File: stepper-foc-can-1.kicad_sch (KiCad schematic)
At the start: 33 parts, among them J1 TC2030, J2 Conn_01x02, J4 Conn_01x04_Pin, U1 STM32G474RBTx, U2 MX25947, Y1 Crystal_GND24

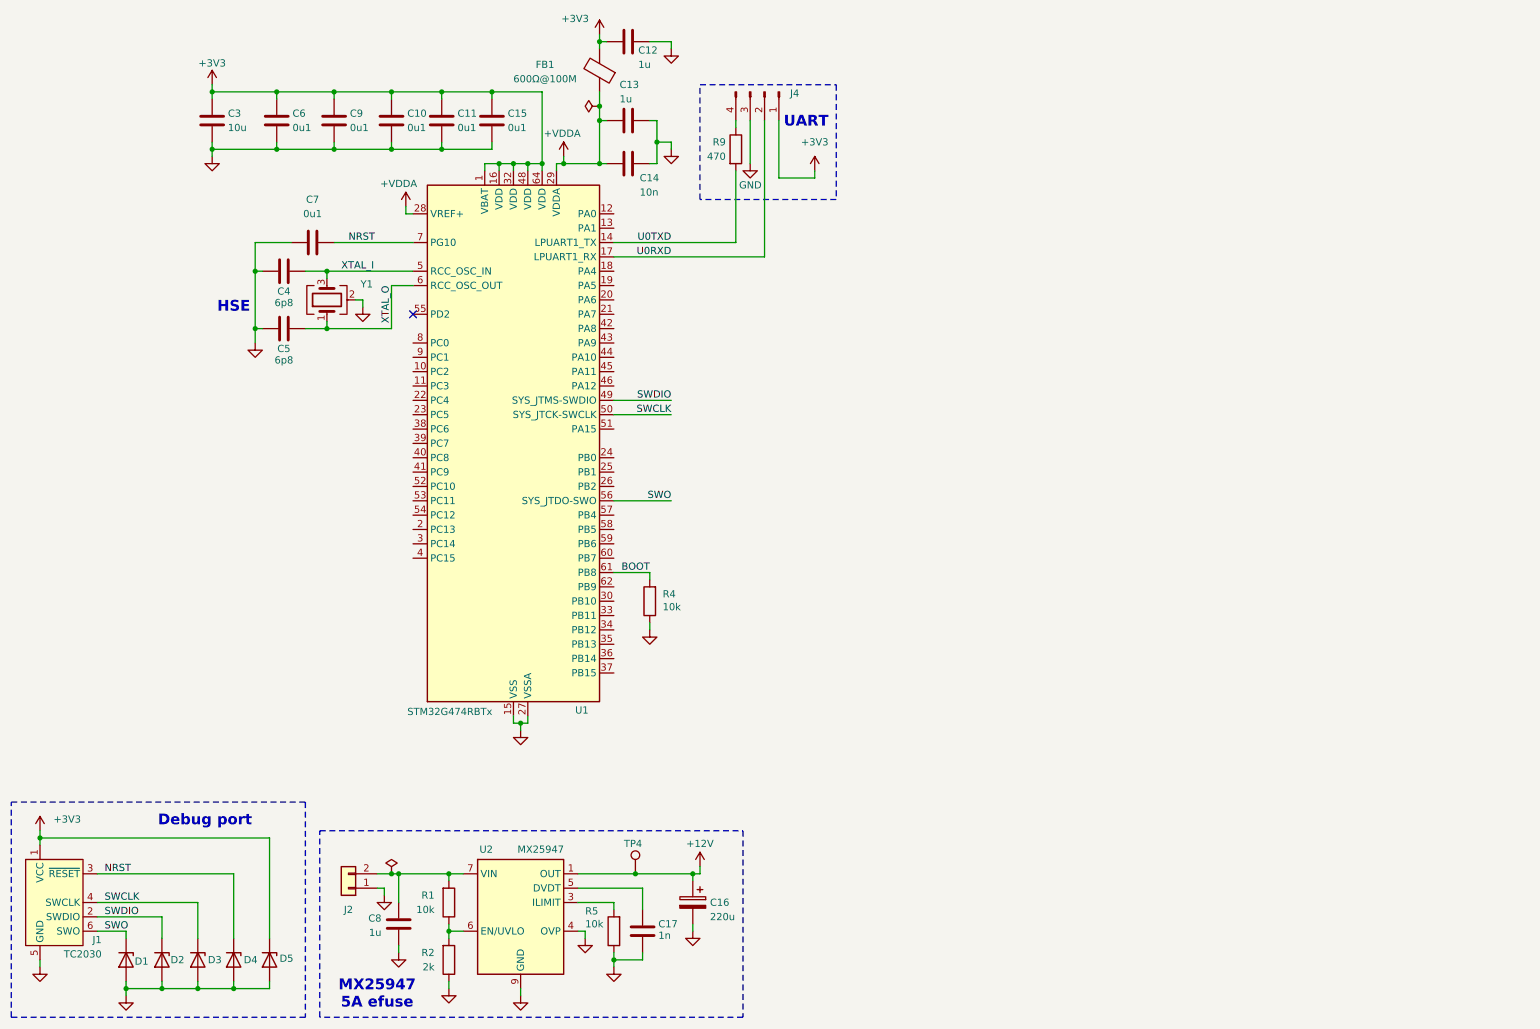
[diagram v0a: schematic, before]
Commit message: schem: import TCAN3413 CAN Transceiver
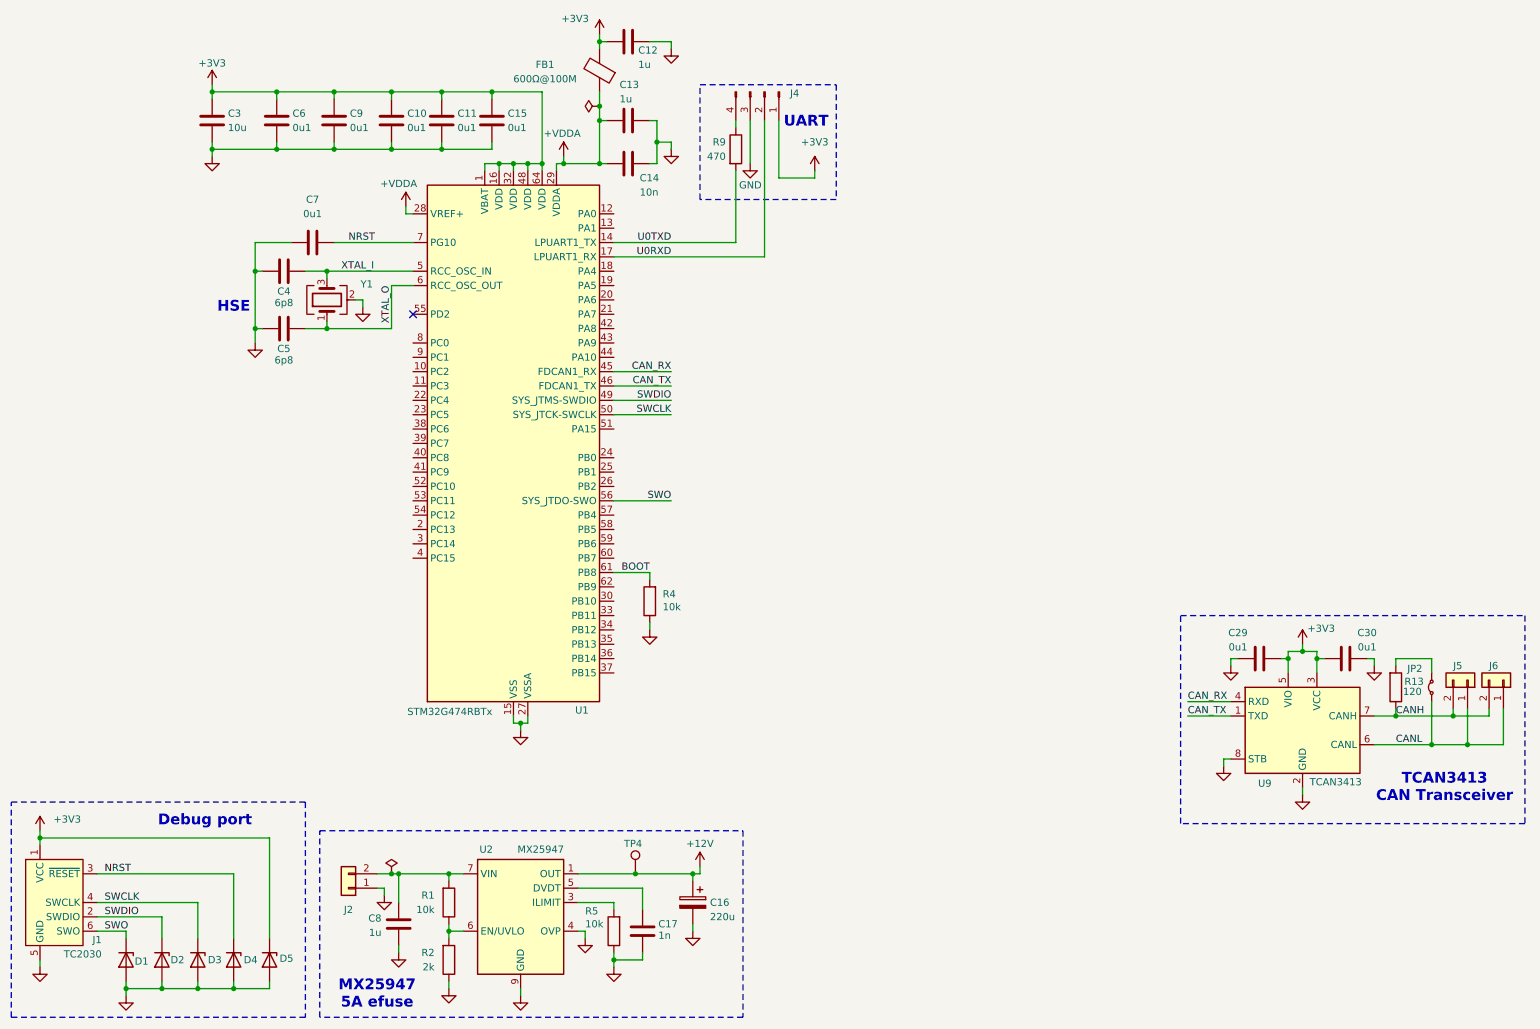
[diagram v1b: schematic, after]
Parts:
- added C29, C30: 0u1, Capacitor_SMD:C_0402_1005Metric, symbol Device:C
- added J5, J6: Conn_01x02, Connector_JST:JST_XH_B2B-XH-A_1x02_P2.50mm_Vertical, symbol Connector_Generic:Conn_01x02
- added JP2: Jumper_2_Small_Bridged, Connector_PinHeader_2.54mm:PinHeader_1x02_P2.54mm_Horizontal, symbol Jumper:Jumper_2_Small_Bridged
- added R13: 120, Resistor_SMD:R_1206_3216Metric, symbol Device:R
- added U9: TCAN3413, Package_TO_SOT_SMD:TSOT-23-8, symbol Interface_CAN_LIN:TCAN334
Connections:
- net +3V3: now also C29.1, C30.1, U9.3 (VCC), U9.5 (VIO)
- net GND: now also C29.2, C30.2, U9.2 (GND), U9.8 (STB)
- net CAN_RX: now reaches U1.45 (PA11)
- net CAN_RX: now also U9.4 (RXD)
- net CAN_TX: now reaches U1.46 (PA12)
- net CAN_TX: now also U9.1 (TXD)
- new net: JP2.2 (B), R13.2
- new net CANH: J5.2 (Pin_2), J6.2 (Pin_2), R13.1, U9.7 (CANH)
- new net CANL: J5.1 (Pin_1), J6.1 (Pin_1), JP2.1 (A), U9.6 (CANL)
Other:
- note added: "TCAN3413 CAN Transceiver"

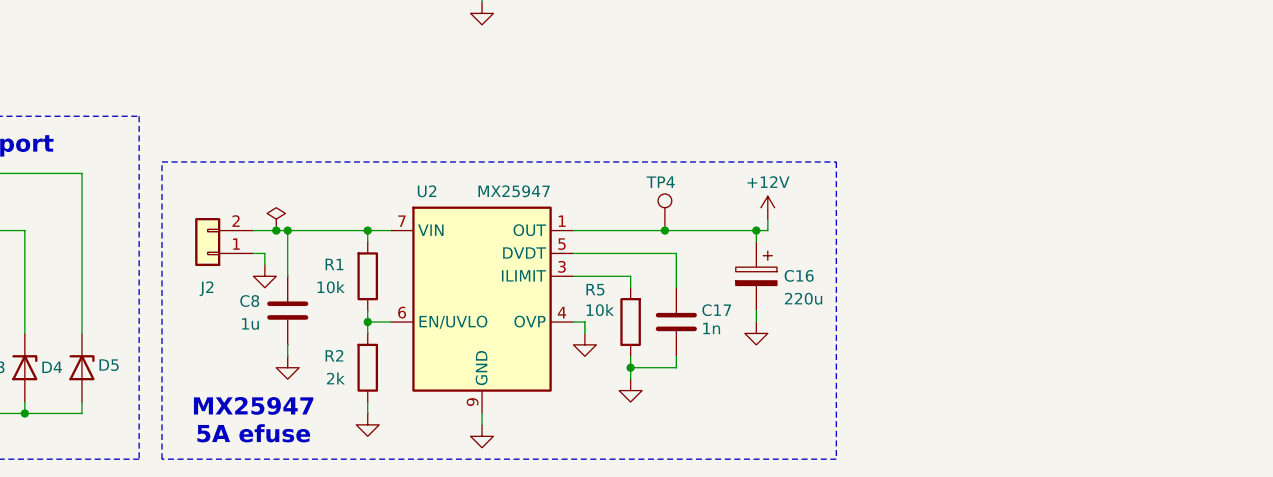
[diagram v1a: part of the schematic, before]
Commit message: schem: add btns
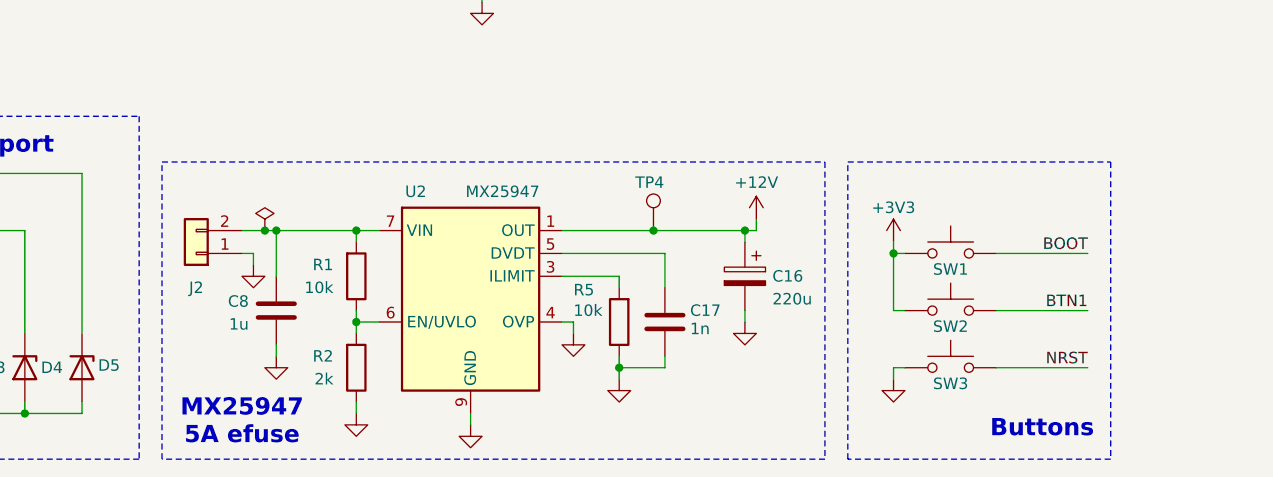
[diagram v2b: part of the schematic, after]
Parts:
- added SW1, SW2, SW3: SW_Push, Button_Switch_SMD:SW_SPST_TS-1088-xR020, symbol Switch:SW_Push
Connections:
- net +3V3: now also SW1.1, SW2.1
- net BOOT: now also SW1.2
- net GND: now also SW3.1
- net NRST: now also SW3.2
- new net BTN1: SW2.2
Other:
- note added: "Buttons"
- moved on the sheet: C16, C17, C8, J2, R1, R2, R5, TP4, U2

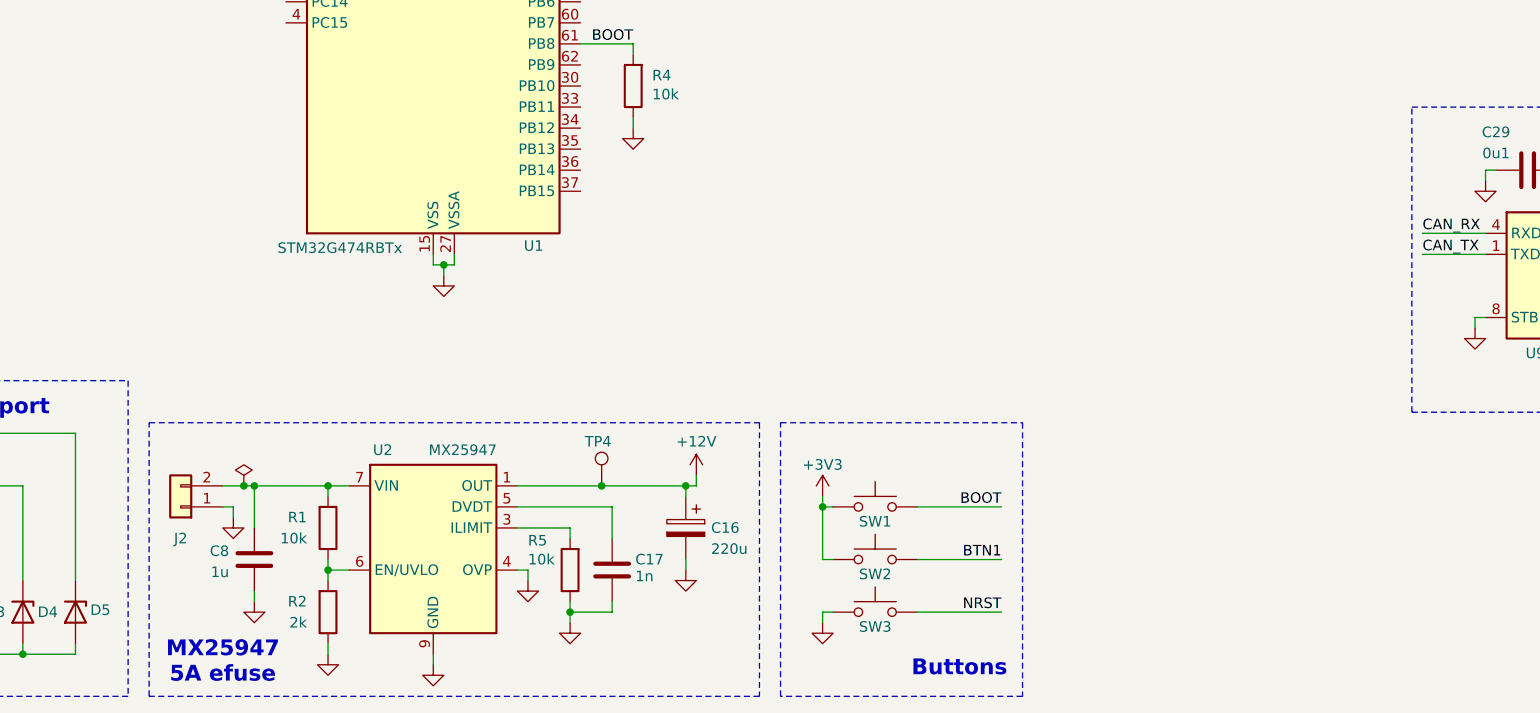
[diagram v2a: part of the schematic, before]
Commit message: schem: add TPS62933 3V3 buck
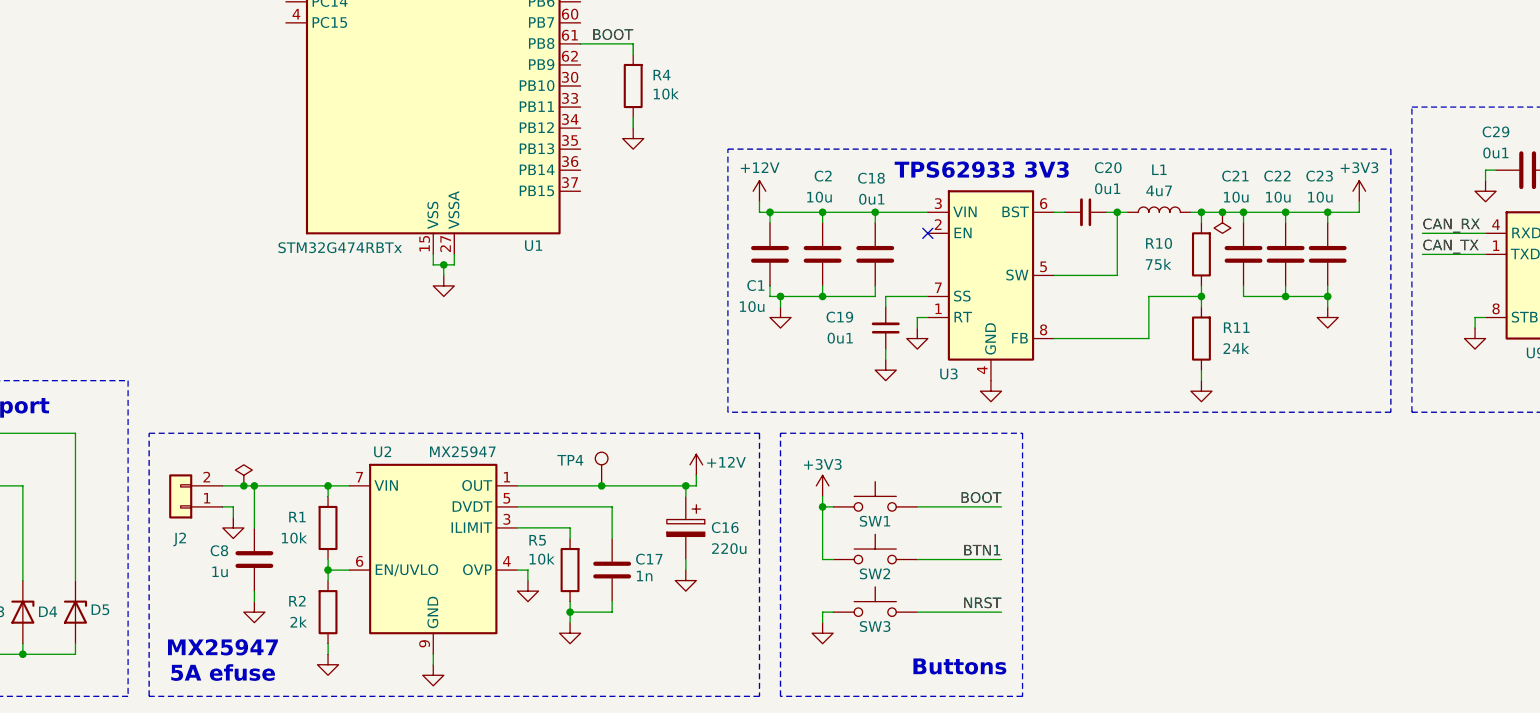
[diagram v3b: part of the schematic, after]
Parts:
- added C1, C2, C21, C22, C23: 10u, Capacitor_SMD:C_0805_2012Metric, symbol Device:C
- added C18: 0u1, Capacitor_SMD:C_0402_1005Metric, symbol Device:C
- added C19, C20: 0u1, Capacitor_SMD:C_0402_1005Metric, symbol Device:C_Small
- added L1: 4u7, Inductor_SMD:L_1008_2520Metric, symbol Device:L
- added R10: 75k, Resistor_SMD:R_0402_1005Metric, symbol Device:R
- added R11: 24k, Resistor_SMD:R_0402_1005Metric, symbol Device:R
- added U3: TPS62933, Package_TO_SOT_SMD:SOT-583-8, symbol Regulator_Switching:TPS62933
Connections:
- net +12V: now also C1.1, C18.1, C2.1, U3.3 (VIN)
- net +3V3: now also C21.1, C22.1, C23.1, L1.2, R10.2
- net GND: now also C1.2, C18.2, C19.1, C2.2, C21.2, C22.2, C23.2, R11.1, U3.1 (RT), U3.4 (GND)
- new net: C20.1, L1.1, U3.5 (SW)
- new net: C20.2, U3.6 (BST)
- new net: C19.2, U3.7 (SS)
- new net: R10.1, R11.2, U3.8 (FB)
- no-connect marks 1 -> 2
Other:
- note added: "TPS62933 3V3"

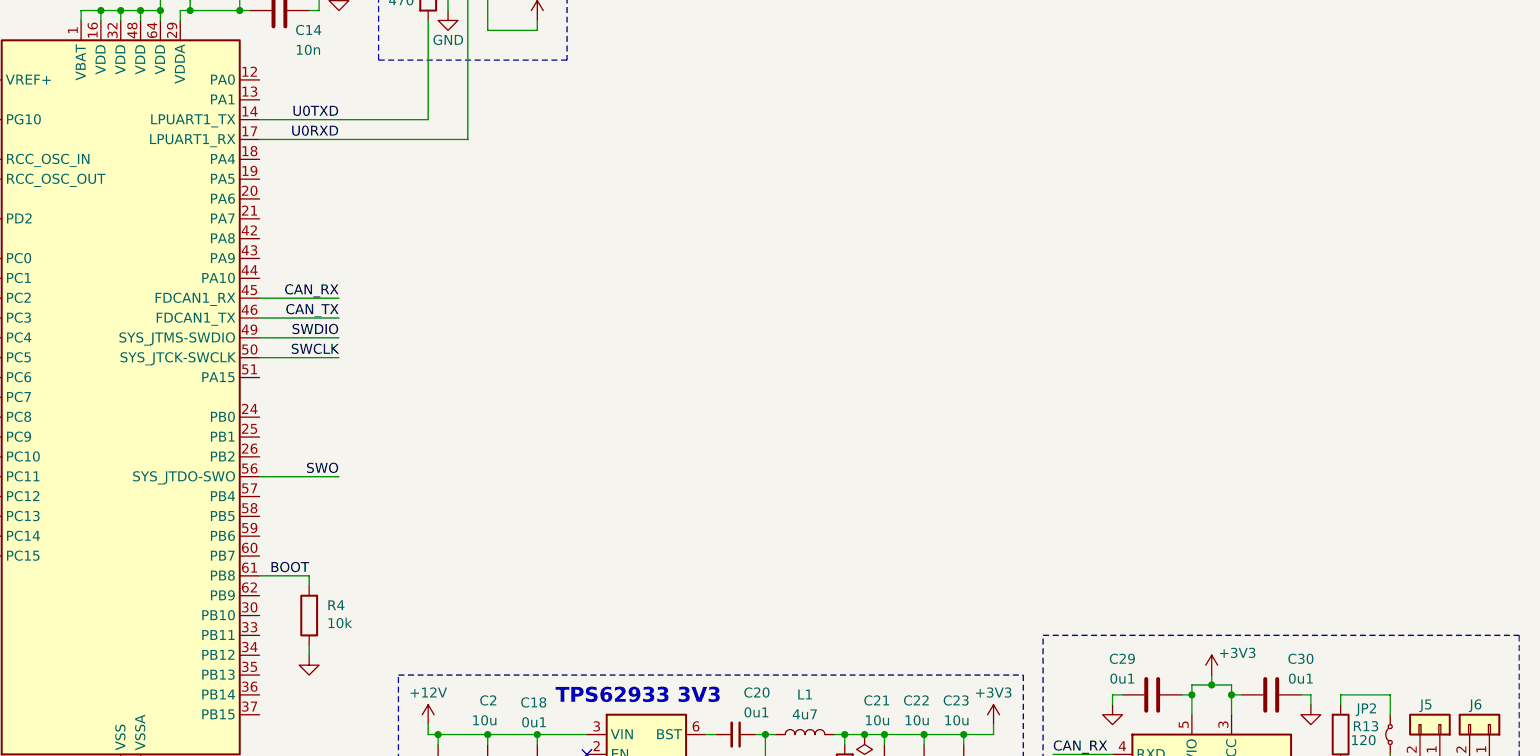
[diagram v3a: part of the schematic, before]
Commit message: schem: add AS5047P Hall Sensor
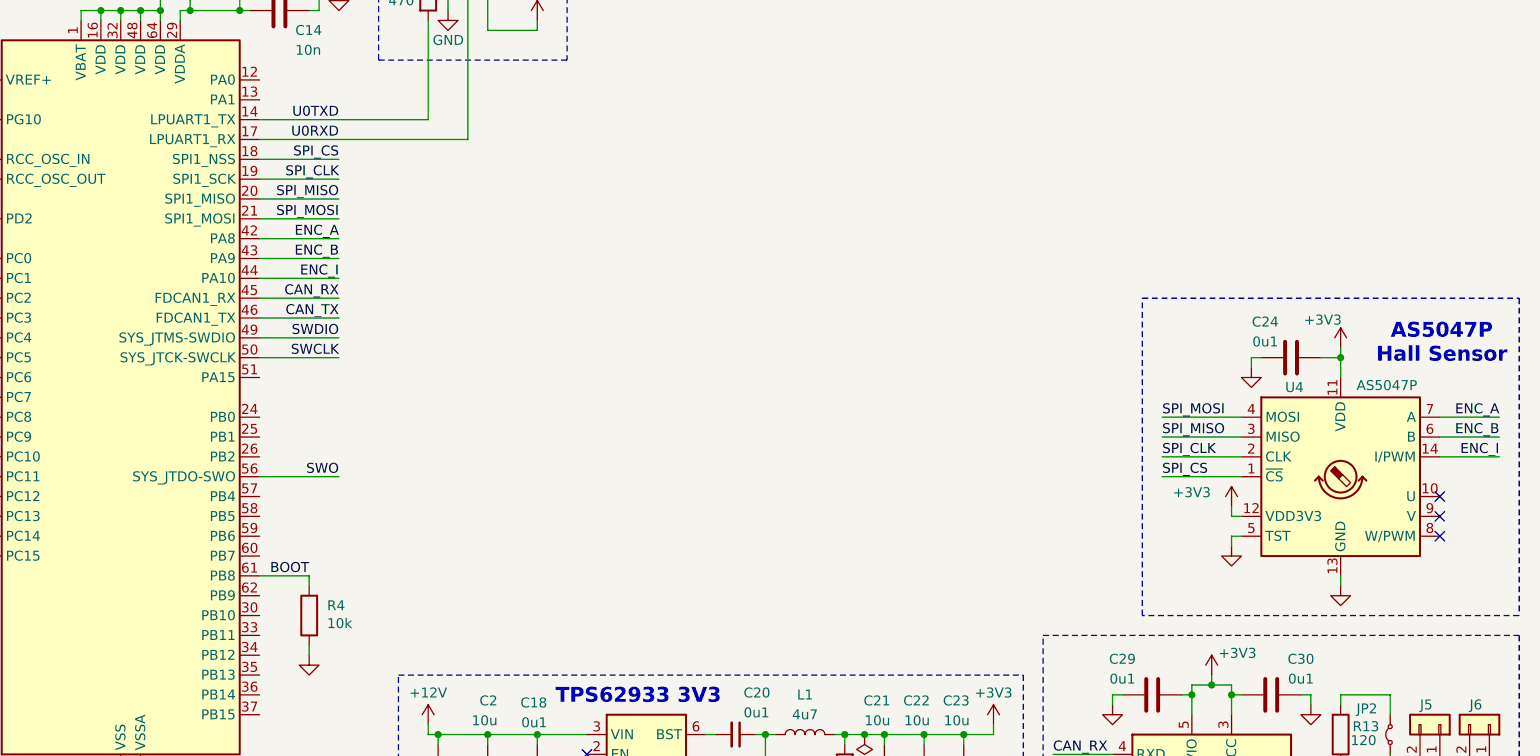
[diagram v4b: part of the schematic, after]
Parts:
- added C24: 0u1, Capacitor_SMD:C_0402_1005Metric, symbol Device:C
- added U4: AS5047P, Package_SO:TSSOP-14_4.4x5mm_P0.65mm, symbol Sensor_Magnetic:AS5047D
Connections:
- net +3V3: now also C24.1, U4.11 (VDD), U4.12 (VDD3V3)
- net GND: now also C24.2, U4.13 (GND), U4.5 (TST)
- net SPI_CS: now reaches U1.18 (PA4)
- net SPI_CS: now also U4.1 (~{CS})
- net SPI_CLK: now reaches U1.19 (PA5)
- net SPI_CLK: now also U4.2 (CLK)
- net SPI_MISO: now reaches U1.20 (PA6)
- net SPI_MISO: now also U4.3 (MISO)
- net SPI_MOSI: now reaches U1.21 (PA7)
- net SPI_MOSI: now also U4.4 (MOSI)
- net ENC_A: now reaches U1.42 (PA8)
- net ENC_A: now also U4.7 (A)
- net ENC_B: now reaches U1.43 (PA9)
- net ENC_B: now also U4.6 (B)
- net ENC_I: now reaches U1.44 (PA10)
- net ENC_I: now also U4.14 (I/PWM)
- no-connect marks 2 -> 5
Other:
- note added: "AS5047P Hall Sensor"
